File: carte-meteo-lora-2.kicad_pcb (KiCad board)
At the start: 4 copper layers, 50 x 50 mm, 79 parts, among them J1 USB_C_Receptacle_USB2.0_14P, J2 Conn_Coaxial, J3 Conn_Coaxial, J4 Conn_Coaxial, J5 Conn_01x04_Pin, SW1 SW_Push, SW2 SW_Push, U1 HS96L03W2C03, U2 SX1262TR8-GC, U3 LDL212PV33R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

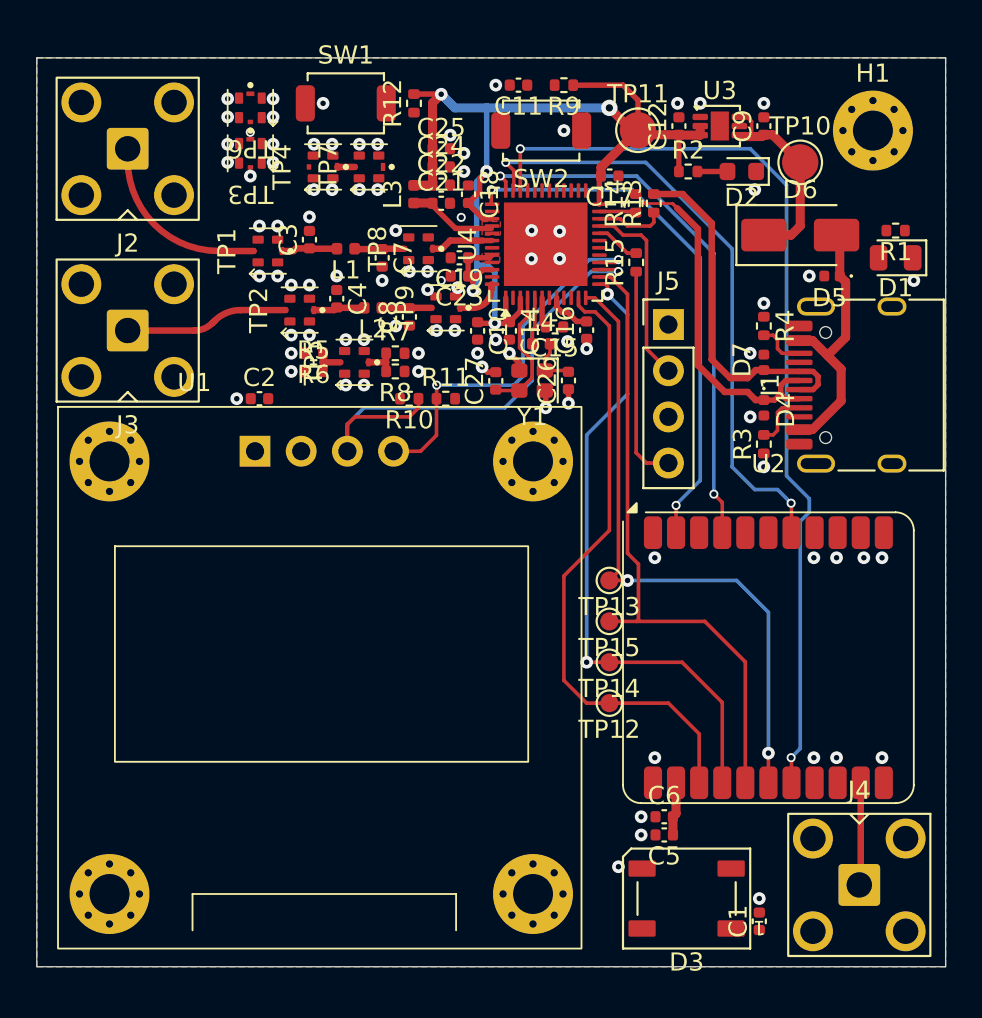
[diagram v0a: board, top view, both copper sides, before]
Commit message: pcb: finish routing 3v3
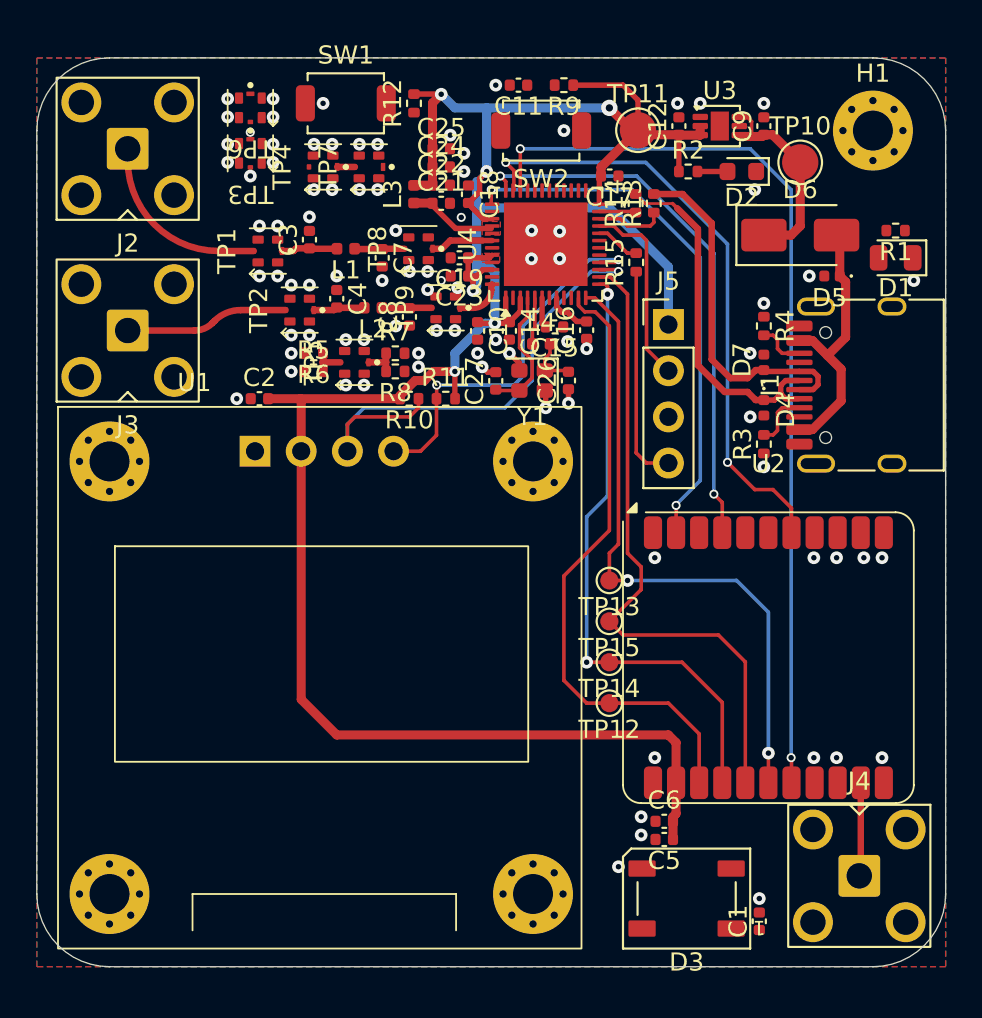
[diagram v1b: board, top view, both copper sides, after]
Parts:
- moved J4 0.50 mm to (139.2, 74.0)
- moved C5 0.25 mm to (128.5, 72.0)
- moved C6 0.25 mm to (128.5, 71.0)
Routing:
- net +3V3: track 70.7 -> 142.5 mm, vias 5 -> 6
- net /MISO: track 35.4 -> 34.4 mm
- net /RST: track 51.6 -> 50.8 mm
- net /MOSI: track 35.3 -> 36.0 mm
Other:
- outline, holes or cut-outs redrawn

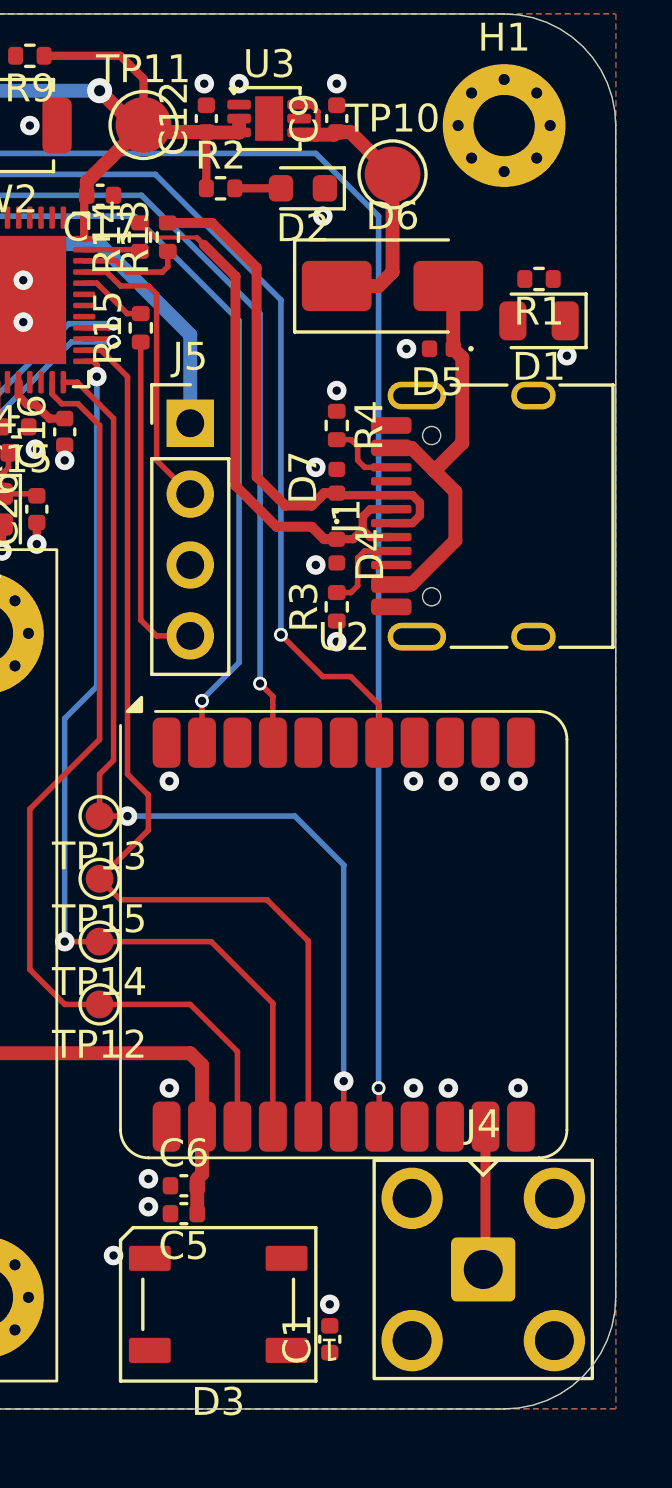
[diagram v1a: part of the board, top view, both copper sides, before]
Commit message: pcb: add +5v pwr routing
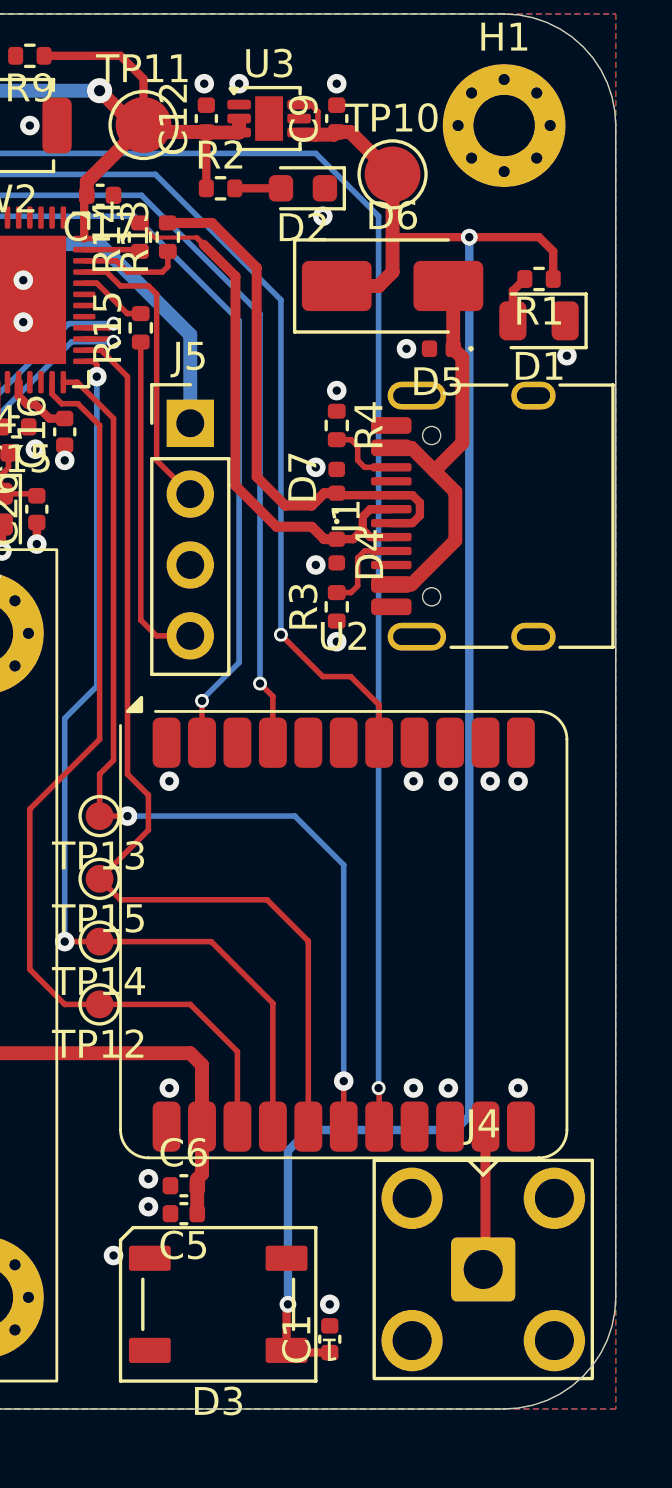
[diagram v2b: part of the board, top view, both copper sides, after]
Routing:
- net +5V_MCU: track 11.4 -> 65.6 mm, vias 0 -> 2
- net Net-(D1-A): track 0.00 -> 1.68 mm
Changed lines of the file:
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@@
+	)
+	(segment
+		(start 140.3125 40)
+		(end 140.3125 38.9275)
+		(width 0.3)
+		(layer "F.Cu")
+		(net "Net-(D1-A)")
+	)
+	(segment
+		(start 140.3125 38.9275)
+		(end 140.74 38.5)
+		(width 0.3)
+		(layer "F.Cu")
+		(net "Net-(D1-A)")
 	)
 	(segment
@@
 	)
 	(segment
+		(start 141.76 37.51)
+		(end 141.76 38.5)
+		(width 0.3)
+		(layer "F.Cu")
+		(net "+5V_MCU")
+	)
+	(segment
 		(start 134.48 33.23)
 		(end 134 33.23)
@@
 	)
 	(segment
+		(start 138.75 37)
+		(end 136 37)
+		(width 0.3)
+		(layer "F.Cu")
+		(net "+5V_MCU")
+	)
+	(segment
 		(start 136 34.75)
 		(end 134.48 33.23)
+		(width 0.5)
+		(layer "F.Cu")
+		(net "+5V_MCU")
+	)
+	(segment
+		(start 136 38.25)
+		(end 136 37)
 		(width 0.5)
 		(layer "F.Cu")
@@
 	)
 	(segment
+		(start 138.75 37)
+		(end 141.25 37)
+		(width 0.3)
+		(layer "F.Cu")
+		(net "+5V_MCU")
+	)
+	(segment
+		(start 132.2 76.9)
+		(end 132.2 75.3)
+		(width 0.3)
+		(layer "F.Cu")
+		(net "+5V_MCU")
+	)
+	(segment
 		(start 132.65 32.25)
 		(end 133.074999 32.25)
@@
 	)
 	(segment
-		(start 136 38.25)
+		(start 136 37)
 		(end 136 34.75)
 		(width 0.5)
@@
 		(net "+5V_MCU")
 	)
+	(segment
+		(start 132.2 75.3)
+		(end 132.25 75.25)
+		(width 0.3)
+		(layer "F.Cu")
+		(net "+5V_MCU")
+	)
+	(segment
+		(start 132.28 76.98)
+		(end 132.2 76.9)
+		(width 0.3)
+		(layer "F.Cu")
+		(net "+5V_MCU")
+	)
+	(segment
+		(start 133.75 76.98)
+		(end 132.28 76.98)
+		(width 0.3)
+		(layer "F.Cu")
+		(net "+5V_MCU")
+	)
+	(segment
+		(start 141.25 37)
+		(end 141.76 37.51)
+		(width 0.3)
+		(layer "F.Cu")
+		(net "+5V_MCU")
+	)
+	(via
+		(at 132.25 75.25)
+		(size 0.6)
+		(drill 0.3)
+		(layers "F.Cu" "B.Cu")
+		(net "+5V_MCU")
+	)
+	(via
+		(at 138.75 37)
+		(size 0.6)
+		(drill 0.3)
+		(layers "F.Cu" "B.Cu")
+		(net "+5V_MCU")
+	)
+	(segment
+		(start 138.25 69)
+		(end 138.75 68.5)
+		(width 0.3)
+		(layer "B.Cu")
+		(net "+5V_MCU")
+	)
+	(segment
+		(start 132.25 69.75)
+		(end 133 69)
+		(width 0.3)
+		(layer "B.Cu")
+		(net "+5V_MCU")
+	)
+	(segment
+		(start 133 69)
+		(end 138.25 69)
+		(width 0.3)
+		(layer "B.Cu")
+		(net "+5V_MCU")
+	)
+	(segment
+		(start 138.75 68.5)
+		(end 138.75 37)
+		(width 0.3)
+		(layer "B.Cu")
+		(net "+5V_MCU")
+	)
+	(segment
+		(start 132.25 75.25)
+		(end 132.25 69.75)
+		(width 0.3)
+		(layer "B.Cu")
+		(net "+5V_MCU")
+	)

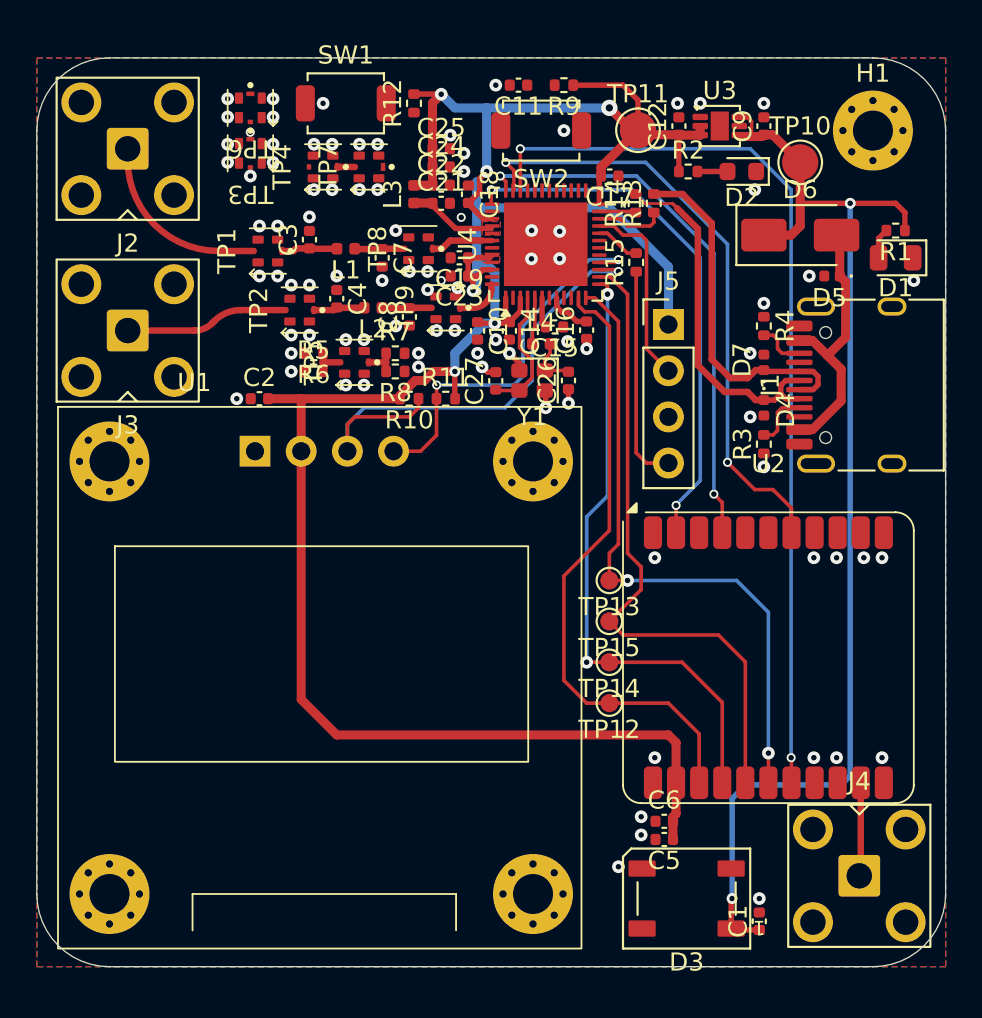
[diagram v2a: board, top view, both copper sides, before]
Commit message: pcb: route boot and rst
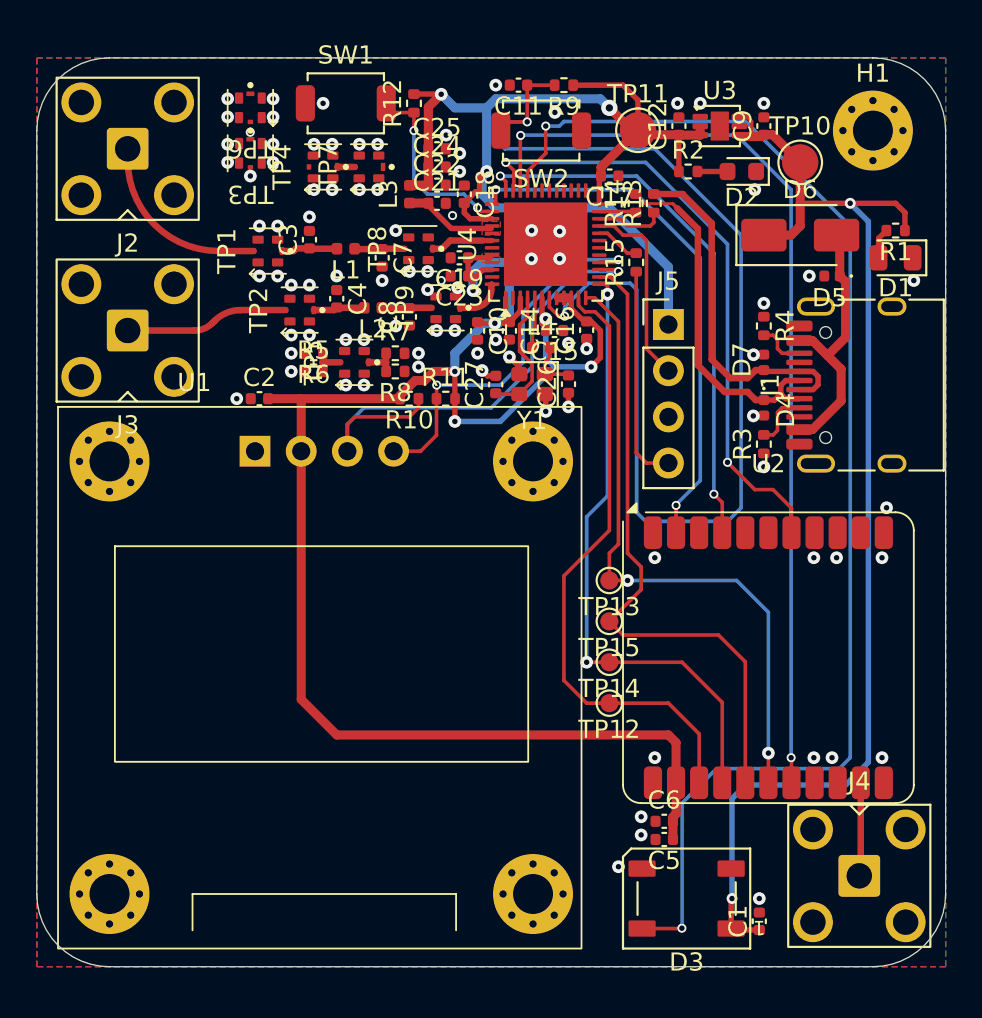
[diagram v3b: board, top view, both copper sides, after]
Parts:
- moved C18 0.23 mm to (117.5, 36.5)
- moved C21 0.23 mm to (116.0, 37.0)
- moved C22 0.23 mm to (116.0, 36.0)
- moved C24 0.23 mm to (116.0, 35.0)
- moved C25 0.23 mm to (116.0, 34.0)
- moved L3 0.23 mm to (114.5, 36.5)
- moved C15 0.20 mm to (122.5, 44.0)
- moved C26 0.20 mm to (123.2, 47.0)
- moved L4 0.20 mm to (121.8, 44.9)
- moved Y1 0.20 mm to (121.2, 47.0)
- moved C27 0.20 mm to (119.2, 47.0)
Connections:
- U4 pad 10: unconnected-(U4-GPIO1/XTAL_32K_N/ADC1_CH0-Pad10) -> +3V3
- U4 pad 9: unconnected-(U4-GPIO0/XTAL_32K_P-Pad9) -> +3V3
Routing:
- net /RGB1: track 0.00 -> 71.8 mm, vias 0 -> 2
- net /CHIP_PU: track 0.00 -> 63.3 mm, vias 0 -> 2
- net +3V3: track 142.5 -> 160.9 mm, vias 6 -> 9
- net /BOOT: track 0.00 -> 10.5 mm, vias 0 -> 2
- net /RST: track 50.8 -> 51.8 mm
- net +5V_MCU: track 65.6 -> 66.6 mm

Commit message: pcb: clean up traces
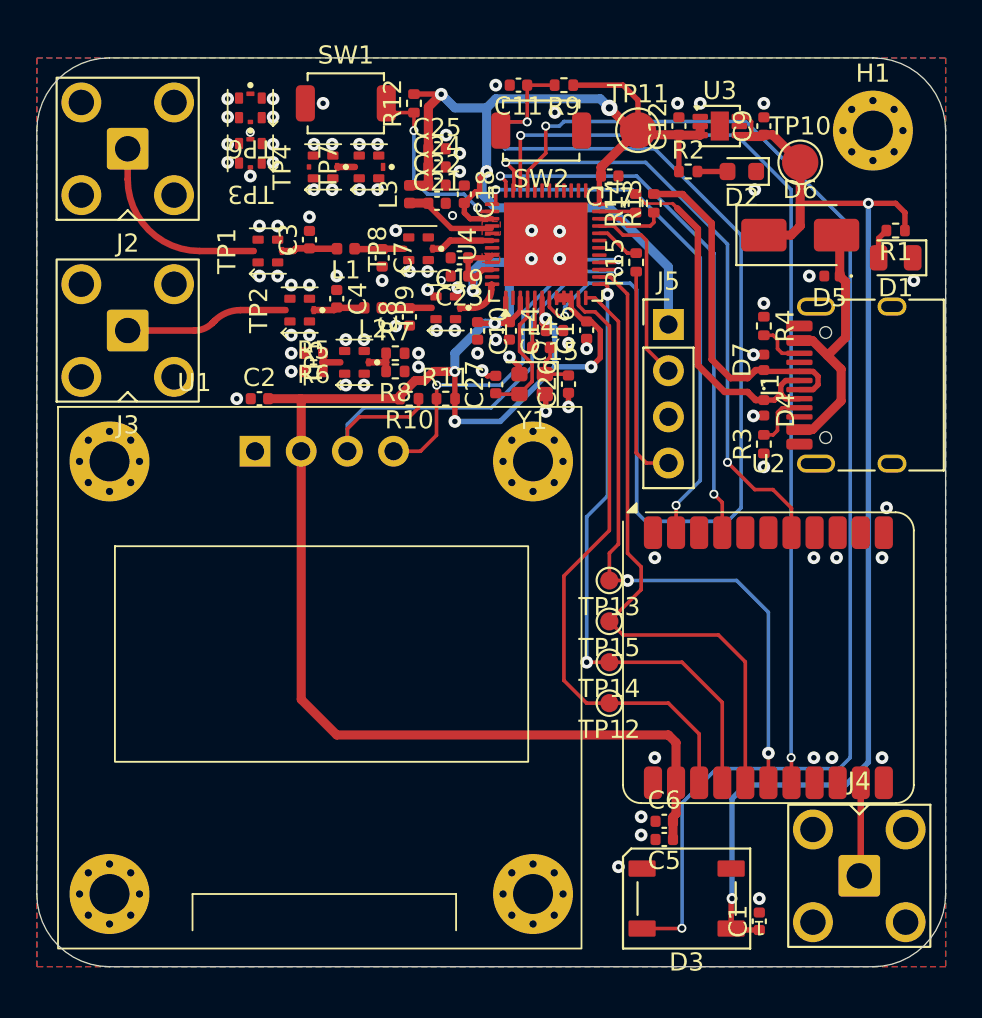
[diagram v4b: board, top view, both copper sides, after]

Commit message: pcb: add stitching vias
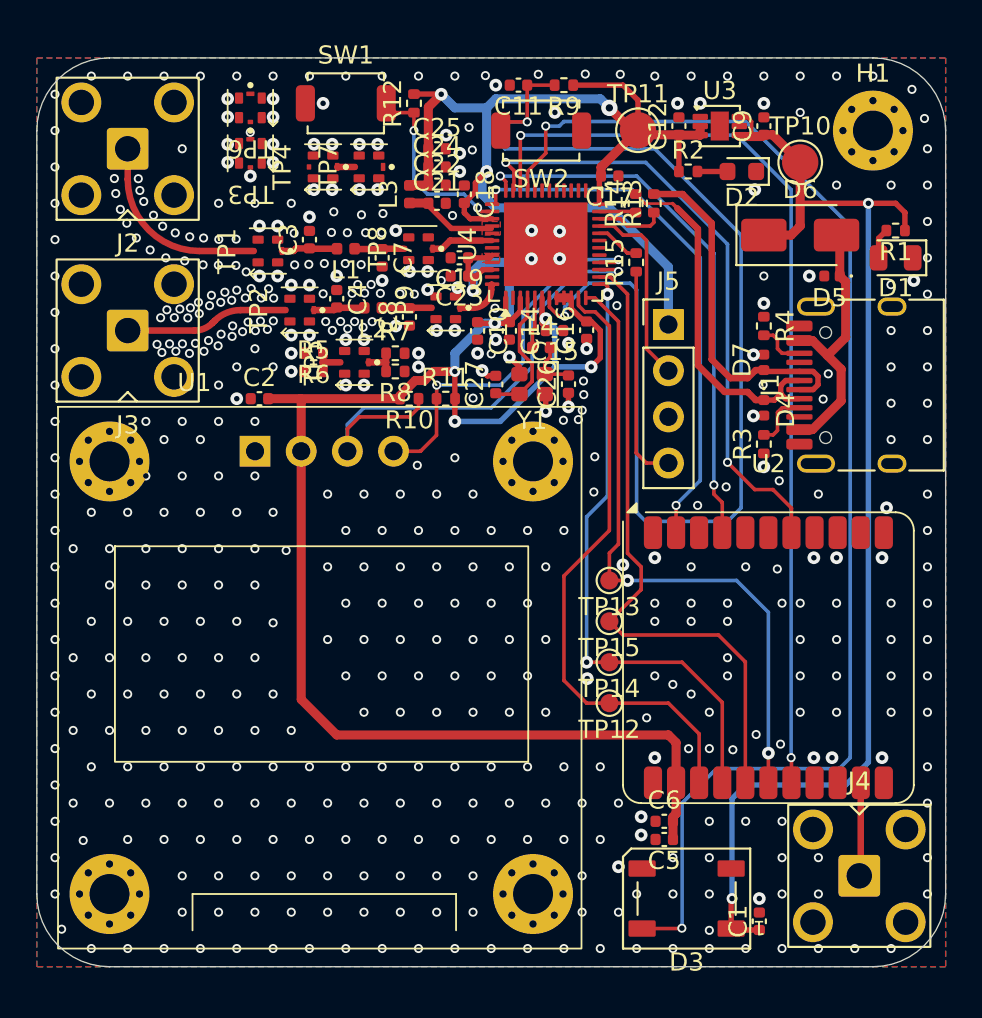
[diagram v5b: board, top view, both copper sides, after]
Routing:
- net GND: vias 89 -> 520

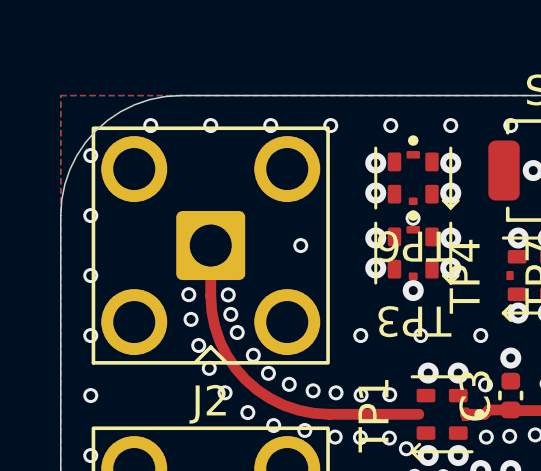
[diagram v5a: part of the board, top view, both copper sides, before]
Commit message: pcb: run and fix DRC
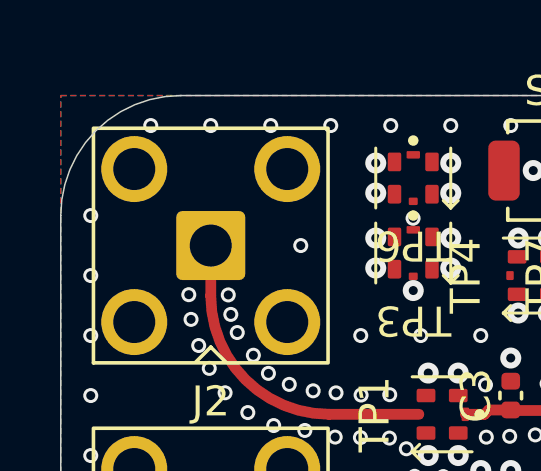
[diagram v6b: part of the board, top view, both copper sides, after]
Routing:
- net GND: vias 520 -> 519
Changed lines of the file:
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@@
-	)
-	(via
-		(at 95 31)
-		(size 0.5)
-		(drill 0.3)
-		(layers "F.Cu" "B.Cu")
-		(free yes)
-		(net "GND")
 	)
 	(via
